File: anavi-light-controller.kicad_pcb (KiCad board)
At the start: 2 copper layers, 74.9 x 40.6 mm, 27 parts, among them J1 Screw_Terminal_1x04, P1 CONN_01X03, Q1 IRF8721PBF-1, Q2 IRF8721PBF-1, Q3 IRF8721PBF-1, SW1 SW_DIP_x01, U1 I2C_SENS_1, U2 I2C_SENS_1, U3 I2C_SENS_1

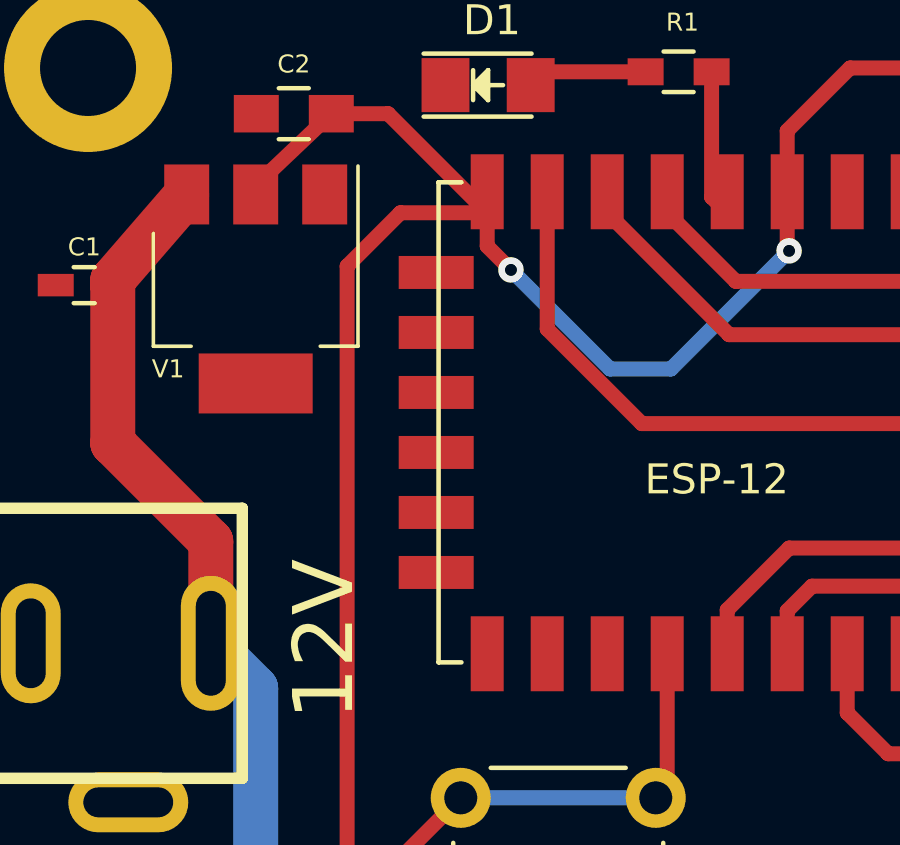
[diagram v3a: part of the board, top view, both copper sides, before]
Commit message: ESP-12E_SMD.kicad_mod: Remove silkscreen from pads
Remove white silkscreen line from pads.

Signed-off-by: Leon Anavi <leon@anavi.org>
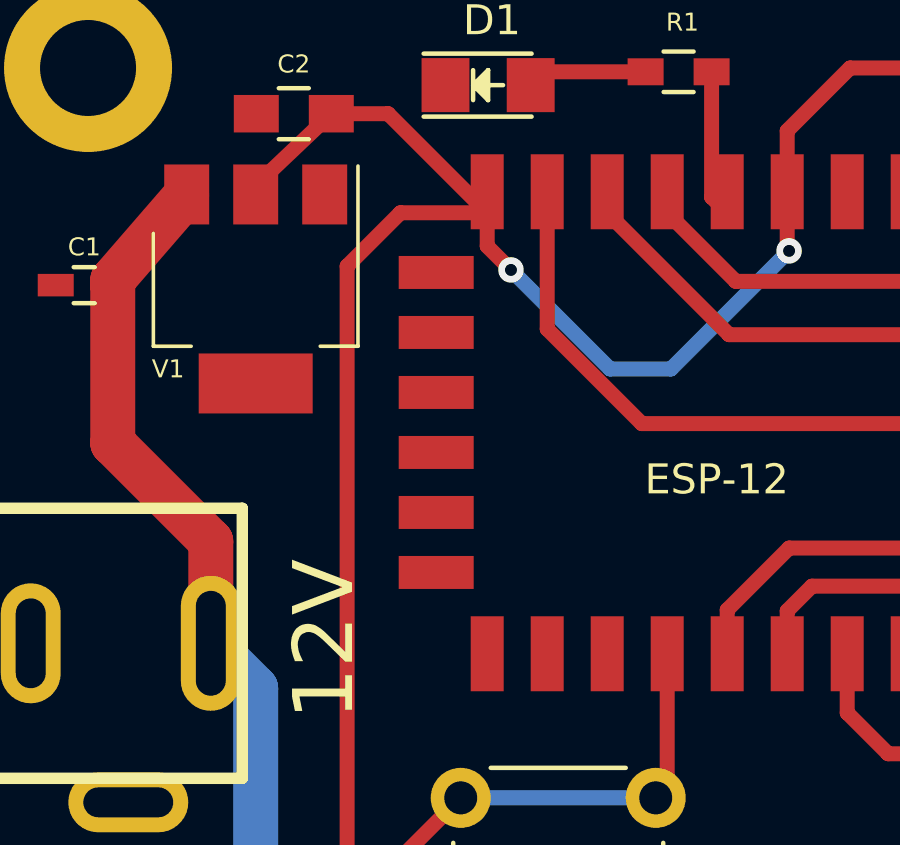
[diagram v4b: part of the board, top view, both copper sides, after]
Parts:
- ESP-12: footprint ESP8266:ESP-12E_SMD -> ESP-12E_SMD
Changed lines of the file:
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@@
     (add_net +12V)
+  )
+  (module ESP-12E_SMD (layer F.Cu)
+    (at 97.155 81.026 270)
+    (descr "Module, ESP-8266, ESP-12, 16 pad, SMD")
+    (tags "Module ESP-8266 ESP8266")
+    (fp_text reference ESP-12 (at 8.89 6.35 360) (layer F.SilkS)
+      (effects (font (size 1 1) (thickness 0.15)))
+    )
+    (fp_text value ESP-12E (at 5.08 6.35 360) (layer F.Fab) hide
+      (effects (font (size 1 1) (thickness 0.15)))
+    )
+    (fp_line (start -2.25 -0.5) (end -2.25 -8.75) (layer F.CrtYd) (width 0.05))
+    (fp_line (start -2.25 -8.75) (end 15.25 -8.75) (layer F.CrtYd) (width 0.05))
+    (fp_line (start 15.25 -8.75) (end 16.25 -8.75) (layer F.CrtYd) (width 0.05))
+    (fp_line (start 16.25 -8.75) (end 16.25 16) (layer F.CrtYd) (width 0.05))
+    (fp_line (start 16.25 16) (end -2.25 16) (layer F.CrtYd) (width 0.05))
+    (fp_line (start -2.25 16) (end -2.25 -0.5) (layer F.CrtYd) (width 0.05))
+    (fp_line (start -1.016 -8.382) (end 14.986 -8.382) (layer F.CrtYd) (width 0.1524))
+    (fp_line (start 14.986 -8.382) (end 14.986 -0.889) (layer F.CrtYd) (width 0.1524))
+    (fp_line (start -1.016 -8.382) (end -1.016 -1.016) (layer F.CrtYd) (width 0.1524))
+    (fp_line (start 14.992 -8.4) (end -1.008 -2.6) (layer F.CrtYd) (width 0.1524))
+    (fp_line (start -1.008 -8.4) (end 14.992 -2.6) (layer F.CrtYd) (width 0.1524))
+    (fp_text user "No Copper" (at 6.892 -5.4 270) (layer F.CrtYd)
+      (effects (font (size 1 1) (thickness 0.15)))
+    )
+    (fp_line (start -1.008 -2.6) (end 14.992 -2.6) (layer F.CrtYd) (width 0.1524))
+    (fp_line (start 15 -8.4) (end 15 15.6) (layer F.Fab) (width 0.05))
+    (fp_line (start 14.992 15.6) (end -1.008 15.6) (layer F.Fab) (width 0.05))
+    (fp_line (start -1.008 15.6) (end -1.008 -8.4) (layer F.Fab) (width 0.05))
+    (fp_line (start -1.008 -8.4) (end 14.992 -8.4) (layer F.Fab) (width 0.05))
+    (pad 1 smd rect (at 0 0 270) (size 2.5 1.1) (drill (offset -0.7 0)) (layers F.Cu F.Paste F.Mask))
+    (pad 2 smd rect (at 0 2 270) (size 2.5 1.1) (drill (offset -0.7 0)) (layers F.Cu F.Paste F.Mask))
+    (pad 3 smd rect (at 0 4 270) (size 2.5 1.1) (drill (offset -0.7 0)) (layers F.Cu F.Paste F.Mask)
+      (net 6 +3V3))
+    (pad 4 smd rect (at 0 6 270) (size 2.5 1.1) (drill (offset -0.7 0)) (layers F.Cu F.Paste F.Mask)
+      (net 18 "Net-(ESP-12-Pad4)"))
+    (pad 5 smd rect (at 0 8 270) (size 2.5 1.1) (drill (offset -0.7 0)) (layers F.Cu F.Paste F.Mask)
+      (net 10 "Net-(ESP-12-Pad5)"))
+    (pad 6 smd rect (at 0 10 270) (size 2.5 1.1) (drill (offset -0.7 0)) (layers F.Cu F.Paste F.Mask)
+      (net 11 "Net-(ESP-12-Pad6)"))
+    (pad 7 smd rect (at 0 12 270) (size 2.5 1.1) (drill (offset -0.7 0)) (layers F.Cu F.Paste F.Mask)
+      (net 12 "Net-(ESP-12-Pad7)"))
+    (pad 8 smd rect (at 0 14 270) (size 2.5 1.1) (drill (offset -0.7 0)) (layers F.Cu F.Paste F.Mask)
+      (net 6 +3V3))
+    (pad 9 smd rect (at 14 14 270) (size 2.5 1.1) (drill (offset 0.7 0)) (layers F.Cu F.Paste F.Mask)
+      (net 2 GND))
+    (pad 10 smd rect (at 14 12 270) (size 2.5 1.1) (drill (offset 0.7 0)) (layers F.Cu F.Paste F.Mask)
+      (net 2 GND))
+    (pad 11 smd rect (at 14 10 270) (size 2.5 1.1) (drill (offset 0.7 0)) (layers F.Cu F.Paste F.Mask))
+    (pad 12 smd rect (at 14 8 270) (size 2.5 1.1) (drill (offset 0.7 0)) (layers F.Cu F.Paste F.Mask)
+      (net 19 "Net-(ESP-12-Pad12)"))
+    (pad 13 smd rect (at 14 6 270) (size 2.5 1.1) (drill (offset 0.7 0)) (layers F.Cu F.Paste F.Mask)
+      (net 7 "Net-(ESP-12-Pad13)"))
+    (pad 14 smd rect (at 14 4 270) (size 2.5 1.1) (drill (offset 0.7 0)) (layers F.Cu F.Paste F.Mask)
+      (net 8 "Net-(ESP-12-Pad14)"))
+    (pad 15 smd rect (at 14 2 270) (size 2.5 1.1) (drill (offset 0.7 0)) (layers F.Cu F.Paste F.Mask)
+      (net 13 "Net-(ESP-12-Pad15)"))
+    (pad 16 smd rect (at 14 0 270) (size 2.5 1.1) (drill (offset 0.7 0)) (layers F.Cu F.Paste F.Mask)
+      (net 14 "Net-(ESP-12-Pad16)"))
+    (pad 17 smd rect (at 1.99 15) (size 2.5 1.1) (drill (offset -0.7 0)) (layers F.Cu F.Paste F.Mask))
+    (pad 18 smd rect (at 3.99 15) (size 2.5 1.1) (drill (offset -0.7 0)) (layers F.Cu F.Paste F.Mask))
+    (pad 19 smd rect (at 5.99 15) (size 2.5 1.1) (drill (offset -0.7 0)) (layers F.Cu F.Paste F.Mask))
+    (pad 20 smd rect (at 7.99 15) (size 2.5 1.1) (drill (offset -0.7 0)) (layers F.Cu F.Paste F.Mask))
+    (pad 21 smd rect (at 9.99 15) (size 2.5 1.1) (drill (offset -0.7 0)) (layers F.Cu F.Paste F.Mask))
+    (pad 22 smd rect (at 11.99 15) (size 2.5 1.1) (drill (offset -0.7 0)) (layers F.Cu F.Paste F.Mask))
+    (model ${ESPLIB}/ESP8266.3dshapes/ESP-12.wrl
+      (at (xyz 0 0 0))
+      (scale (xyz 0.3937 0.3937 0.3937))
+      (rotate (xyz 0 0 0))
+    )
   )
   (module SOT-223 (layer F.Cu)
@@
       (rotate (xyz 0 0 0))
     )
-  )
-  (module ESP8266:ESP-12E_SMD (layer F.Cu)
-    (at 97.155 81.026 270)
-    (descr "Module, ESP-8266, ESP-12, 16 pad, SMD")
-    (tags "Module ESP-8266 ESP8266")
-    (fp_text reference ESP-12 (at 8.89 6.35 360) (layer F.SilkS)
-      (effects (font (size 1 1) (thickness 0.15)))
-    )
-    (fp_text value ESP-12E (at 5.08 6.35 360) (layer F.Fab) hide
-      (effects (font (size 1 1) (thickness 0.15)))
-    )
-    (fp_line (start -2.25 -0.5) (end -2.25 -8.75) (layer F.CrtYd) (width 0.05))
-    (fp_line (start -2.25 -8.75) (end 15.25 -8.75) (layer F.CrtYd) (width 0.05))
-    (fp_line (start 15.25 -8.75) (end 16.25 -8.75) (layer F.CrtYd) (width 0.05))
-    (fp_line (start 16.25 -8.75) (end 16.25 16) (layer F.CrtYd) (width 0.05))
-    (fp_line (start 16.25 16) (end -2.25 16) (layer F.CrtYd) (width 0.05))
-    (fp_line (start -2.25 16) (end -2.25 -0.5) (layer F.CrtYd) (width 0.05))
-    (fp_line (start -1.016 -8.382) (end 14.986 -8.382) (layer F.CrtYd) (width 0.1524))
-    (fp_line (start 14.986 -8.382) (end 14.986 -0.889) (layer F.CrtYd) (width 0.1524))
-    (fp_line (start -1.016 -8.382) (end -1.016 -1.016) (layer F.CrtYd) (width 0.1524))
-    (fp_line (start -1.016 14.859) (end -1.016 15.621) (layer F.SilkS) (width 0.1524))
-    (fp_line (start -1.016 15.621) (end 14.986 15.621) (layer F.SilkS) (width 0.1524))
-    (fp_line (start 14.986 15.621) (end 14.986 14.859) (layer F.SilkS) (width 0.1524))
-    (fp_line (start 14.992 -8.4) (end -1.008 -2.6) (layer F.CrtYd) (width 0.1524))
-    (fp_line (start -1.008 -8.4) (end 14.992 -2.6) (layer F.CrtYd) (width 0.1524))
-    (fp_text user "No Copper" (at 6.892 -5.4 270) (layer F.CrtYd)
-      (effects (font (size 1 1) (thickness 0.15)))
-    )
-    (fp_line (start -1.008 -2.6) (end 14.992 -2.6) (layer F.CrtYd) (width 0.1524))
-    (fp_line (start 15 -8.4) (end 15 15.6) (layer F.Fab) (width 0.05))
-    (fp_line (start 14.992 15.6) (end -1.008 15.6) (layer F.Fab) (width 0.05))
-    (fp_line (start -1.008 15.6) (end -1.008 -8.4) (layer F.Fab) (width 0.05))
-    (fp_line (start -1.008 -8.4) (end 14.992 -8.4) (layer F.Fab) (width 0.05))
-    (pad 1 smd rect (at 0 0 270) (size 2.5 1.1) (drill (offset -0.7 0)) (layers F.Cu F.Paste F.Mask))
-    (pad 2 smd rect (at 0 2 270) (size 2.5 1.1) (drill (offset -0.7 0)) (layers F.Cu F.Paste F.Mask))
-    (pad 3 smd rect (at 0 4 270) (size 2.5 1.1) (drill (offset -0.7 0)) (layers F.Cu F.Paste F.Mask)
-      (net 6 +3V3))
-    (pad 4 smd rect (at 0 6 270) (size 2.5 1.1) (drill (offset -0.7 0)) (layers F.Cu F.Paste F.Mask)
-      (net 18 "Net-(ESP-12-Pad4)"))
-    (pad 5 smd rect (at 0 8 270) (size 2.5 1.1) (drill (offset -0.7 0)) (layers F.Cu F.Paste F.Mask)
-      (net 10 "Net-(ESP-12-Pad5)"))
-    (pad 6 smd rect (at 0 10 270) (size 2.5 1.1) (drill (offset -0.7 0)) (layers F.Cu F.Paste F.Mask)
-      (net 11 "Net-(ESP-12-Pad6)"))
-    (pad 7 smd rect (at 0 12 270) (size 2.5 1.1) (drill (offset -0.7 0)) (layers F.Cu F.Paste F.Mask)
-      (net 12 "Net-(ESP-12-Pad7)"))
-    (pad 8 smd rect (at 0 14 270) (size 2.5 1.1) (drill (offset -0.7 0)) (layers F.Cu F.Paste F.Mask)
-      (net 6 +3V3))
-    (pad 9 smd rect (at 14 14 270) (size 2.5 1.1) (drill (offset 0.7 0)) (layers F.Cu F.Paste F.Mask)
-      (net 2 GND))
-    (pad 10 smd rect (at 14 12 270) (size 2.5 1.1) (drill (offset 0.7 0)) (layers F.Cu F.Paste F.Mask)
-      (net 2 GND))
-    (pad 11 smd rect (at 14 10 270) (size 2.5 1.1) (drill (offset 0.7 0)) (layers F.Cu F.Paste F.Mask))
-    (pad 12 smd rect (at 14 8 270) (size 2.5 1.1) (drill (offset 0.7 0)) (layers F.Cu F.Paste F.Mask)
-      (net 19 "Net-(ESP-12-Pad12)"))
-    (pad 13 smd rect (at 14 6 270) (size 2.5 1.1) (drill (offset 0.7 0)) (layers F.Cu F.Paste F.Mask)
-      (net 7 "Net-(ESP-12-Pad13)"))
-    (pad 14 smd rect (at 14 4 270) (size 2.5 1.1) (drill (offset 0.7 0)) (layers F.Cu F.Paste F.Mask)
-      (net 8 "Net-(ESP-12-Pad14)"))
-    (pad 15 smd rect (at 14 2 270) (size 2.5 1.1) (drill (offset 0.7 0)) (layers F.Cu F.Paste F.Mask)
-      (net 13 "Net-(ESP-12-Pad15)"))
-    (pad 16 smd rect (at 14 0 270) (size 2.5 1.1) (drill (offset 0.7 0)) (layers F.Cu F.Paste F.Mask)
-      (net 14 "Net-(ESP-12-Pad16)"))
-    (pad 17 smd rect (at 1.99 15) (size 2.5 1.1) (drill (offset -0.7 0)) (layers F.Cu F.Paste F.Mask))
-    (pad 18 smd rect (at 3.99 15) (size 2.5 1.1) (drill (offset -0.7 0)) (layers F.Cu F.Paste F.Mask))
-    (pad 19 smd rect (at 5.99 15) (size 2.5 1.1) (drill (offset -0.7 0)) (layers F.Cu F.Paste F.Mask))
-    (pad 20 smd rect (at 7.99 15) (size 2.5 1.1) (drill (offset -0.7 0)) (layers F.Cu F.Paste F.Mask))
-    (pad 21 smd rect (at 9.99 15) (size 2.5 1.1) (drill (offset -0.7 0)) (layers F.Cu F.Paste F.Mask))
-    (pad 22 smd rect (at 11.99 15) (size 2.5 1.1) (drill (offset -0.7 0)) (layers F.Cu F.Paste F.Mask))
-    (model ${ESPLIB}/ESP8266.3dshapes/ESP-12.wrl
-      (at (xyz 0 0 0))
-      (scale (xyz 0.3937 0.3937 0.3937))
-      (rotate (xyz 0 0 0))
-    )

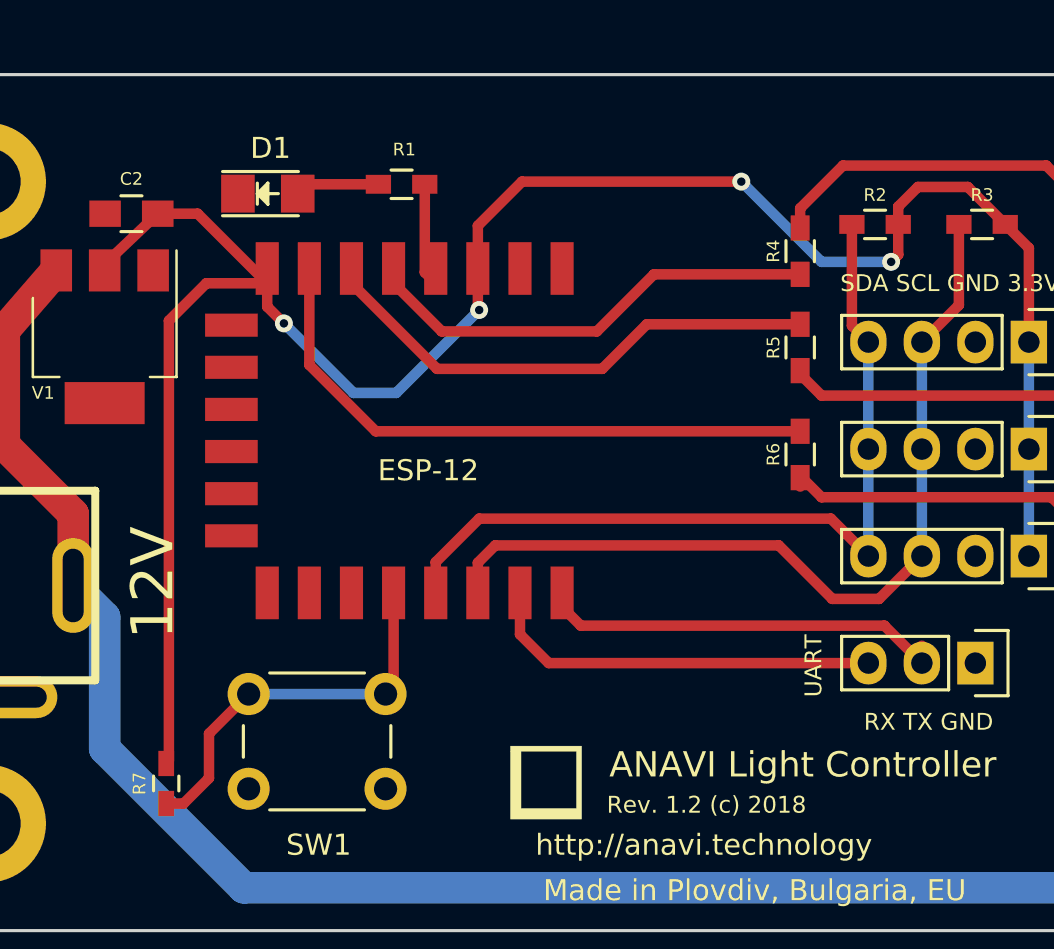
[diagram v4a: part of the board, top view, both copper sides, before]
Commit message: anavi-light-controller.kicad_pcb: Rotate ESP-12E
Rotate ESP8266 model ESP-12E to 90 degrees to
improve the signal strenght of the WiFi antenna
and increase the revision to 1.3.

Huge thanks for the suggested improvements to Jon
Raymond (twitter: @Jon_Raymond_) and John Lee
(twitter: @EspressifSystem).

Signed-off-by: Leon Anavi <leon@anavi.org>
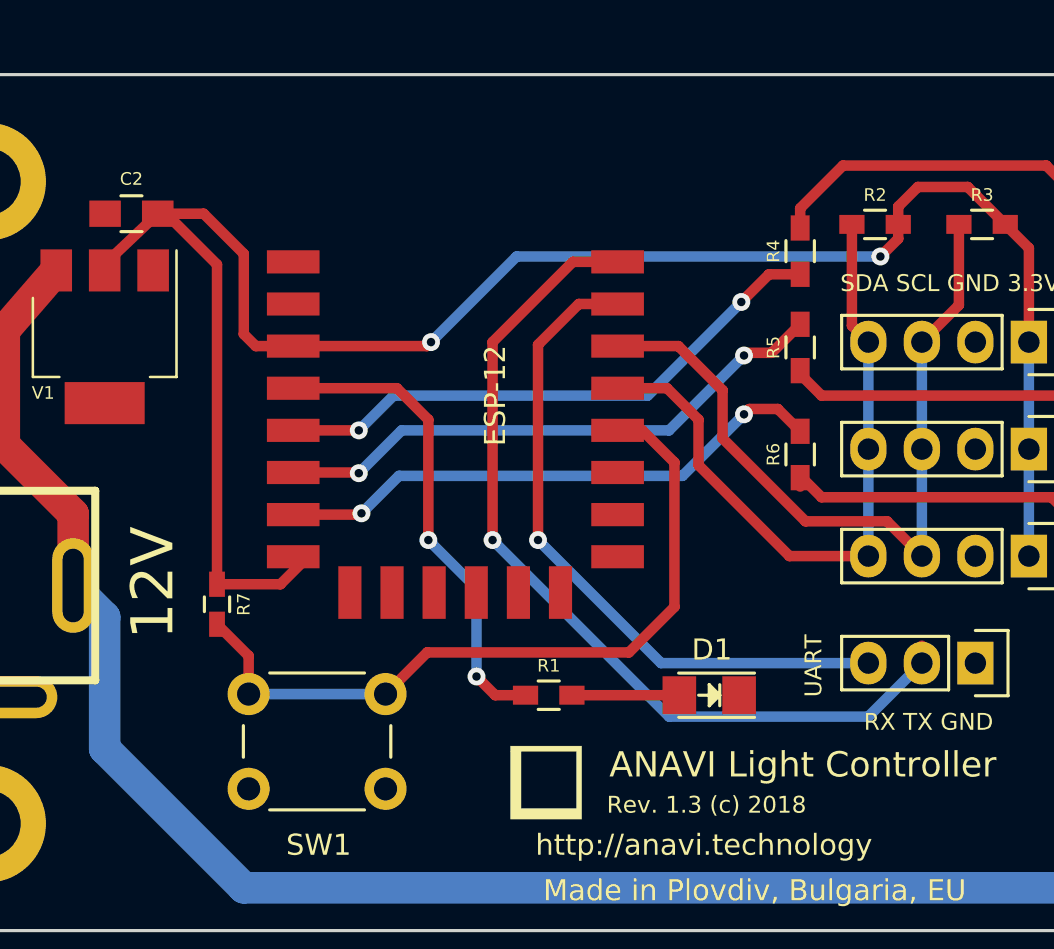
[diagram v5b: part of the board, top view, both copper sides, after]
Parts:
- moved D1 31.7 mm to (104.1, 100.6), turned to 180 degrees
- moved R1 25.2 mm to (96.5, 100.6), turned to 0 degrees
- moved ESP-12 12.1 mm to (85.1, 80.0), turned to 0 degrees
- moved R7 8.84 mm to (80.8, 96.3)
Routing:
- net Net-(ESP-12-Pad16): track 20.4 -> 41.9 mm, vias 0 -> 1
- net Net-(ESP-12-Pad12): track 21.0 -> 38.8 mm
- net Net-(ESP-12-Pad4): track 5.02 -> 22.2 mm, vias 0 -> 2
- net Net-(ESP-12-Pad15): track 19.8 -> 31.3 mm, vias 0 -> 1
- net +3V3: track 104.5 -> 95.6 mm, vias 4 -> 2
- net Net-(ESP-12-Pad13): track 39.3 -> 33.6 mm
- net Net-(ESP-12-Pad5): track 21.7 -> 26.7 mm, vias 0 -> 2
- net Net-(ESP-12-Pad14): track 40.5 -> 37.1 mm
- net Net-(ESP-12-Pad7): track 28.5 -> 25.9 mm, vias 0 -> 2
- net Net-(ESP-12-Pad6): track 23.9 -> 26.3 mm, vias 0 -> 2
- net Net-(D1-Pad2): track 4.55 -> 5.10 mm
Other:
- board text added: "Rev. 1.3 (c) 2018"
- board text removed: "Rev. 1.2 (c) 2018"
